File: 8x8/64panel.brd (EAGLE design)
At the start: 25.4 x 25.4 mm, 72 parts, among them J1 LED_PADCIRCULARPAD, J2 LED_PADCIRCULARPAD, J3 LED_PADCIRCULARPAD, J4 LED_PADCIRCULARPAD, J5 LED_PADCIRCULARPAD, J6 LED_PADCIRCULARPAD, J7 LED_PADCIRCULARPAD, J8 LED_PADCIRCULARPAD

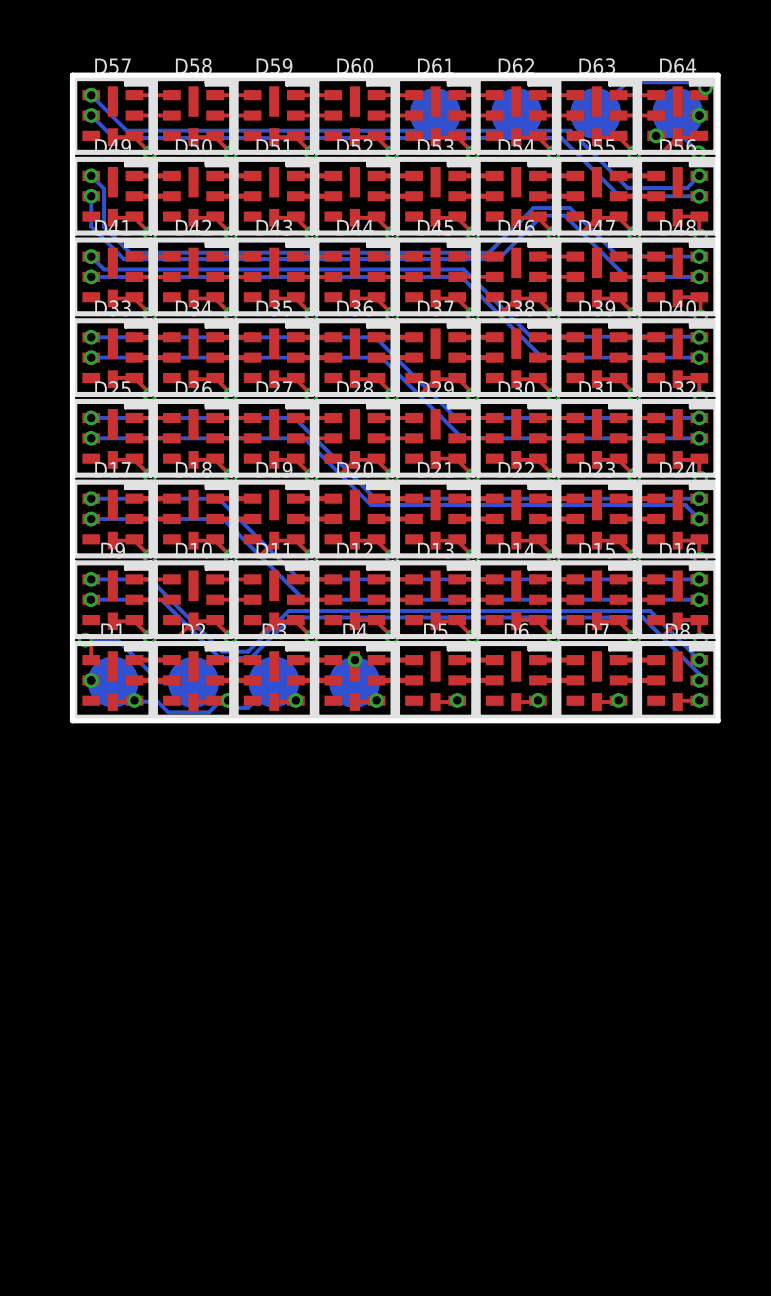
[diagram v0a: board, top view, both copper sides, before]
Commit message: finished laying out board, ordered panels
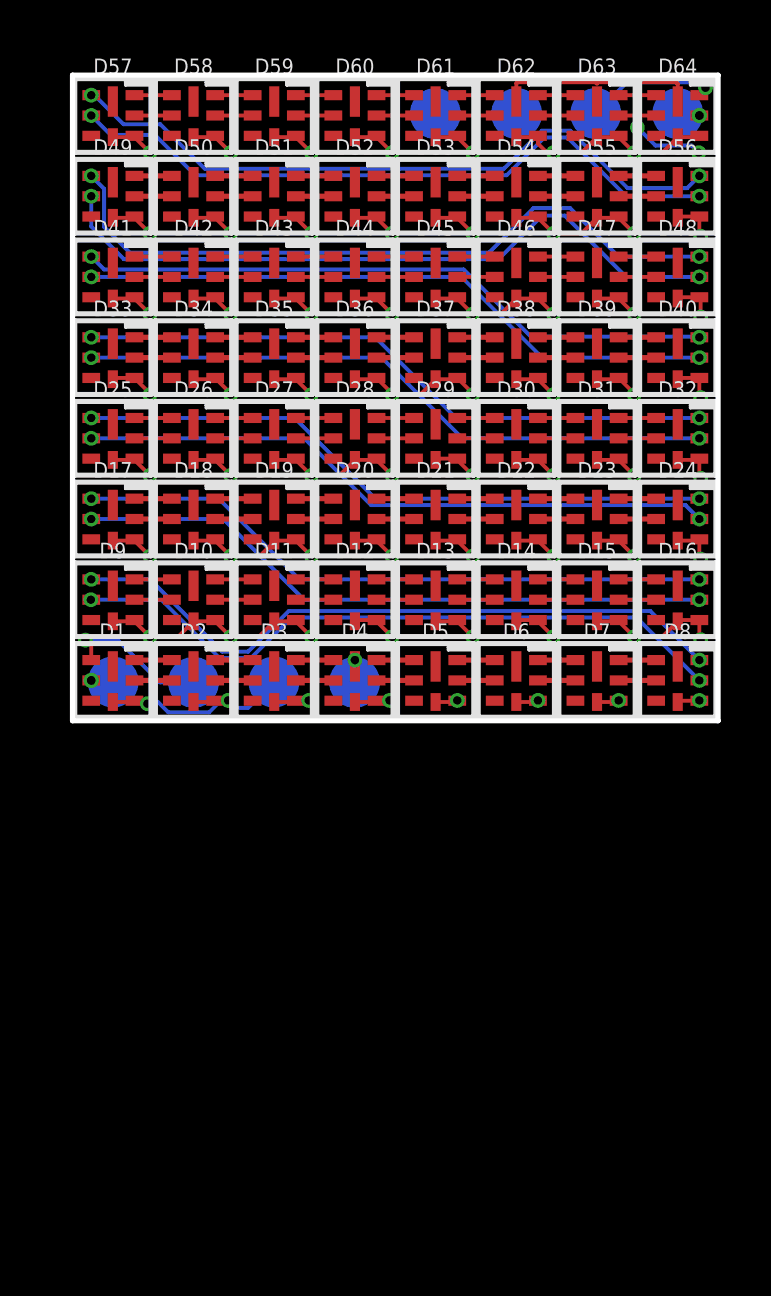
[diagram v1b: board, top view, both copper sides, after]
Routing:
- net GND: track 1.95 -> 10.8 mm
- net 5V: track 130.2 -> 133.8 mm
- net N$103: track 25.6 -> 26.9 mm
- net N$104: track 25.2 -> 26.5 mm

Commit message: changing to 6-pin
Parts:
- added FRAME1: FRAME-LEDGER, SparkFun-Aesthetics:CREATIVE_COMMONS
- added LOGO1: SFE_LOGO_NAME_FLAME.2_INCH, SparkFun-Aesthetics:SFE_LOGO_NAME_FLAME_.2
- added U$1, U$2: (no value), buzzard_labels (4):5V5
- added U$3: (no value), buzzard_labels (4):CI1
- added U$4: (no value), buzzard_labels (4):CO3
- added U$5: (no value), buzzard_labels (4):DI2
- added U$6: (no value), buzzard_labels (4):DO4
- added U$7, U$8: (no value), buzzard_labels (4):GND6
- added U$9: (no value), buzzard_labels (4):LUMINI_8X8_MATRIX0
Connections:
- net 5V: no longer D1.VDDPAD, D10.VDDPAD, D11.VDDPAD, D12.VDDPAD, D13.VDDPAD, D14.VDDPAD, D15.VDDPAD, D16.VDDPAD, D17.VDDPAD, D18.VDDPAD, D19.VDDPAD, D2.VDDPAD, D20.VDDPAD, D21.VDDPAD, D22.VDDPAD, D23.VDDPAD, D24.VDDPAD, D25.VDDPAD, D26.VDDPAD, D27.VDDPAD, D28.VDDPAD, D29.VDDPAD, D3.VDDPAD, D30.VDDPAD, D31.VDDPAD, D32.VDDPAD, D33.VDDPAD, D34.VDDPAD, D35.VDDPAD, D36.VDDPAD, D37.VDDPAD, D38.VDDPAD, D39.VDDPAD, D4.VDDPAD, D40.VDDPAD, D41.VDDPAD, D42.VDDPAD, D43.VDDPAD, D44.VDDPAD, D45.VDDPAD, D46.VDDPAD, D47.VDDPAD, D48.VDDPAD, D49.VDDPAD, D5.VDDPAD, D50.VDDPAD, D51.VDDPAD, D52.VDDPAD, D53.VDDPAD, D54.VDDPAD, D55.VDDPAD, D56.VDDPAD, D57.VDDPAD, D58.VDDPAD, D59.VDDPAD, D6.VDDPAD, D60.VDDPAD, D61.VDDPAD, D62.VDDPAD, D63.VDDPAD, D64.VDDPAD, D7.VDDPAD, D8.VDDPAD, D9.VDDPAD
- net GND: no longer D1.GNDPAD, D10.GNDPAD, D11.GNDPAD, D12.GNDPAD, D13.GNDPAD, D14.GNDPAD, D15.GNDPAD, D16.GNDPAD, D17.GNDPAD, D18.GNDPAD, D19.GNDPAD, D2.GNDPAD, D20.GNDPAD, D21.GNDPAD, D22.GNDPAD, D23.GNDPAD, D24.GNDPAD, D25.GNDPAD, D26.GNDPAD, D27.GNDPAD, D28.GNDPAD, D29.GNDPAD, D3.GNDPAD, D30.GNDPAD, D31.GNDPAD, D32.GNDPAD, D33.GNDPAD, D34.GNDPAD, D35.GNDPAD, D36.GNDPAD, D37.GNDPAD, D38.GNDPAD, D39.GNDPAD, D4.GNDPAD, D40.GNDPAD, D41.GNDPAD, D42.GNDPAD, D43.GNDPAD, D44.GNDPAD, D45.GNDPAD, D46.GNDPAD, D47.GNDPAD, D48.GNDPAD, D49.GNDPAD, D5.GNDPAD, D50.GNDPAD, D51.GNDPAD, D52.GNDPAD, D53.GNDPAD, D54.GNDPAD, D55.GNDPAD, D56.GNDPAD, D57.GNDPAD, D58.GNDPAD, D59.GNDPAD, D6.GNDPAD, D60.GNDPAD, D61.GNDPAD, D62.GNDPAD, D63.GNDPAD, D64.GNDPAD, D7.GNDPAD, D8.GNDPAD, D9.GNDPAD
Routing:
- net 5V: track 133.8 -> 61.6 mm, vias 63 -> 64
- net GND: track 10.8 -> 8.30 mm, vias 3 -> 2
- net N$89: track 27.6 -> 25.4 mm
- net N$90: track 27.4 -> 25.6 mm
- net N$17: track 26.6 -> 25.4 mm
- net N$18: track 26.6 -> 25.6 mm
